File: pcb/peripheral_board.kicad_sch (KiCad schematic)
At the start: 2 parts

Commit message: Continue work on PCBs.
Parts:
- added SW3: SW_RST, Button_Switch_THT:SW_PUSH_6mm, symbol Switch:SW_Push
- added U3: ~, excelsior:MCP23017_Breakout, symbol excelsior:MCP23017_Breakout
- J3, J4: value ~ -> HDMI Breakout
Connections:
- net VBUS: now reaches J4.00 (VBUS)
- net VBUS: now also J3.00 (VBUS), U3.00 (VBUS)
- net MISO: now reaches J4.01 (P01)
- net MISO: now also J3.01 (P01)
- net CS0: now reaches J4.02 (P02)
- net CS0: now also J3.02 (P02)
- net SCK: now reaches J4.03 (P03)
- net SCK: now also J3.03 (P03)
- net CS1: now reaches J4.04 (P04)
- net CS1: now also J3.04 (P04)
- net MOSI: now reaches J4.05 (P05)
- net MOSI: now also J3.05 (P05)
- net CS2: now reaches J4.06 (P06)
- net CS2: now also J3.06 (P06)
- net SDA: now reaches J4.07 (P07)
- net SDA: now also J3.07 (P07), U3.03 (SDA)
- net CS3: now reaches J4.08 (P08)
- net CS3: now also J3.08 (P08)
- net SCL: now reaches J4.09 (P09)
- net SCL: now also J3.09 (P09), U3.02 (SCL)
- net CS4: now reaches J4.10 (P10)
- net CS4: now also J3.10 (P10)
- net INTA1: now reaches J4.11 (P11)
- net INTA1: now also J3.11 (P11), U3.25 (INTA)
- net CS5: now reaches J4.12 (P12)
- net CS5: now also J3.12 (P12)
- net INTB1: now reaches J4.13 (P13)
- net INTB1: now also J3.13 (P13), U3.24 (INTB)
- net CS6: now reaches J4.14 (P14)
- net CS6: now also J3.14 (P14)
- net INTA2: now reaches J4.15 (P15)
- net INTA2: now also J3.15 (P15)
- net CS7: now reaches J4.16 (P16)
- net CS7: now also J3.16 (P16)
- net GND: now reaches J4.G (GND)
- net GND: now also J3.G (GND), SW3.1, U3.01 (GND)
- new net: SW3.2, U3.04 (RST)
- new net C00: U3.20 (GPB0)
- new net C01: U3.19 (GPB1)
- new net C02: U3.18 (GPB2)
- new net C03: U3.17 (GPB3)
- new net C04: U3.16 (GPB4)
- new net C05: U3.15 (GPB5)
- new net GPA6: U3.11 (GPA6)
- new net GPA7: U3.12 (GPA7)
- new net GPB6: U3.14 (GPB6)
- new net GPB7: U3.13 (GPB7)
- new net INTB2: J3.19 (P19), J4.19 (P19)
- new net R00: U3.05 (GPA0)
- new net R01: U3.06 (GPA1)
- new net R02: U3.07 (GPA2)
- new net R03: U3.08 (GPA3)
- new net R04: U3.09 (GPA4)
- new net R05: U3.10 (GPA5)
- no-connect marks 0 -> 3

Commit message: Continue work on PCBs.
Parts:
- J3, J4: value HDMI Breakout -> Pogo Pin Connector; footprint excelsior:HDMI_Breakout -> Connector_PinHeader_2.54mm:PinHeader_1x12_P2.54mm_Vertical; symbol excelsior:HDMI_Breakout -> Connector_Generic:Conn_01x12
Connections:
- net CS4 is gone; now on net CS0: J3.10 (Pin_10), J4.10 (Pin_10)
- net CS5 is gone; now on net CS2: J3.12 (Pin_12), J4.12 (Pin_12)
- net CS0: no longer J3.02 (P02), J4.02 (P02)
- net CS1: now also J3.11 (Pin_11), J4.11 (Pin_11); no longer J3.04 (P04), J4.04 (P04)
- net CS2: no longer J3.06 (P06), J4.06 (P06)
- net GND: no longer J3.G (GND), J4.G (GND)
- net INTA1: now also J3.6 (Pin_6), J4.6 (Pin_6); no longer J3.11 (P11), J4.11 (P11)
- net INTA2: now also J3.8 (Pin_8), J4.8 (Pin_8); no longer J3.15 (P15), J4.15 (P15)
- net INTB1: now also J3.7 (Pin_7), J4.7 (Pin_7); no longer J3.13 (P13), J4.13 (P13)
- net INTB2: now also J3.9 (Pin_9), J4.9 (Pin_9); no longer J3.19 (P19), J4.19 (P19)
- net MISO: now also J3.1 (Pin_1), J4.1 (Pin_1); no longer J3.01 (P01), J4.01 (P01)
- net MOSI: now also J3.3 (Pin_3), J4.3 (Pin_3); no longer J3.05 (P05), J4.05 (P05)
- net SCK: now also J3.2 (Pin_2), J4.2 (Pin_2); no longer J3.03 (P03), J4.03 (P03)
- net SCL: now also J3.5 (Pin_5), J4.5 (Pin_5); no longer J3.09 (P09), J4.09 (P09)
- net SDA: now also J3.4 (Pin_4), J4.4 (Pin_4); no longer J3.07 (P07), J4.07 (P07)
- net VBUS: no longer J3.00 (VBUS), J4.00 (VBUS)
- removed net CS3: J3.08 (P08), J4.08 (P08)
- removed net CS6: J3.14 (P14), J4.14 (P14)
- removed net CS7: J3.16 (P16), J4.16 (P16)

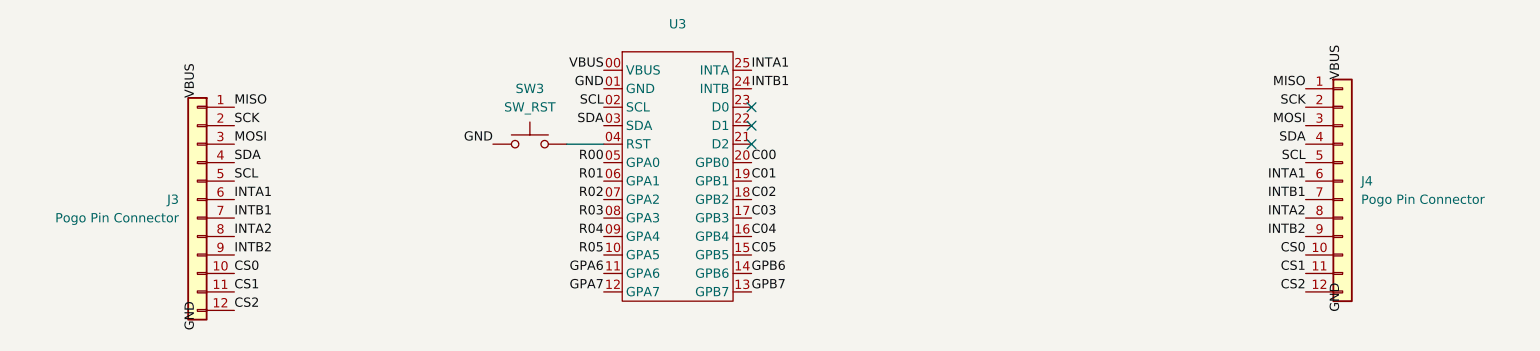
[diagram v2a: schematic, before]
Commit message: - Update main Readme. - Add folders for case CAD and KMK files. - In the PCBs, fix VBUS and GND being removed from connectors. - Add PCB readme.
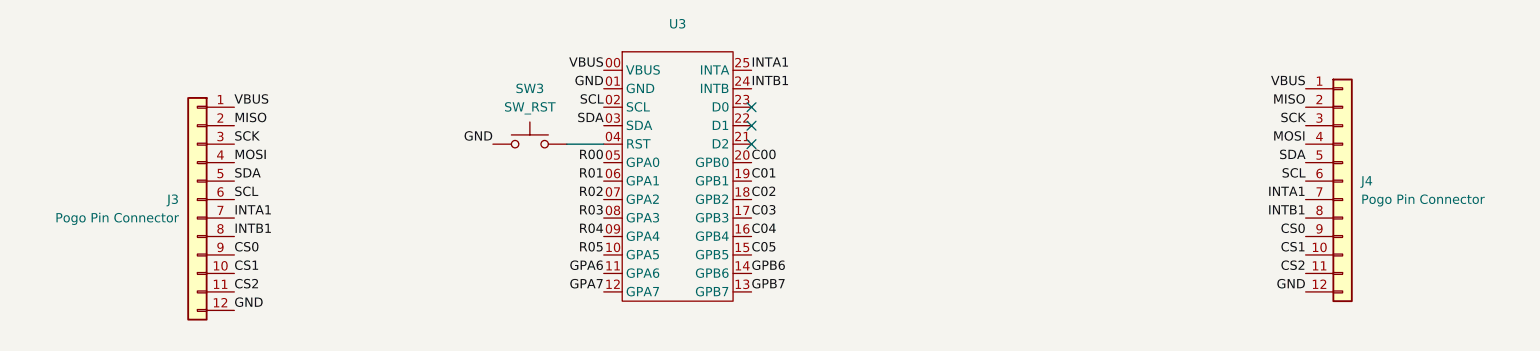
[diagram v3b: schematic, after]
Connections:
- net INTA2 is gone; now on net INTB1: J3.8 (Pin_8), J4.8 (Pin_8)
- net INTB2 is gone; now on net CS0: J3.9 (Pin_9), J4.9 (Pin_9)
- net CS0: no longer J3.10 (Pin_10), J4.10 (Pin_10)
- net CS1: now also J3.10 (Pin_10), J4.10 (Pin_10); no longer J3.11 (Pin_11), J4.11 (Pin_11)
- net CS2: now also J3.11 (Pin_11), J4.11 (Pin_11); no longer J3.12 (Pin_12), J4.12 (Pin_12)
- net GND: now also J3.12 (Pin_12), J4.12 (Pin_12)
- net INTA1: now also J3.7 (Pin_7), J4.7 (Pin_7); no longer J3.6 (Pin_6), J4.6 (Pin_6)
- net INTB1: no longer J3.7 (Pin_7), J4.7 (Pin_7)
- net MISO: now also J3.2 (Pin_2), J4.2 (Pin_2); no longer J3.1 (Pin_1), J4.1 (Pin_1)
- net MOSI: now also J3.4 (Pin_4), J4.4 (Pin_4); no longer J3.3 (Pin_3), J4.3 (Pin_3)
- net SCK: now also J3.3 (Pin_3), J4.3 (Pin_3); no longer J3.2 (Pin_2), J4.2 (Pin_2)
- net SCL: now also J3.6 (Pin_6), J4.6 (Pin_6); no longer J3.5 (Pin_5), J4.5 (Pin_5)
- net SDA: now also J3.5 (Pin_5), J4.5 (Pin_5); no longer J3.4 (Pin_4), J4.4 (Pin_4)
- net VBUS: now also J3.1 (Pin_1), J4.1 (Pin_1)
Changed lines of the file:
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@@
-		)
-	)
-	(label "INTA1"
-		(at 233.68 86.36 180)
-		(effects
-			(font
-				(size 1.27 1.27)
-			)
-			(justify right bottom)
-		)
-	)
-	(label "MOSI"
-		(at 233.68 78.74 180)
-		(effects
-			(font
-				(size 1.27 1.27)
-			)
-			(justify right bottom)
 		)
 	)
@@
 		)
 	)
-	(label "GND"
-		(at 238.76 100.33 270)
-		(effects
-			(font
-				(size 1.27 1.27)
-			)
-			(justify right bottom)
-		)
-	)
-	(label "INTB1"
-		(at 233.68 88.9 180)
-		(effects
-			(font
-				(size 1.27 1.27)
-			)
-			(justify right bottom)
+	(label "INTA1"
+		(at 86.36 91.44 0)
+		(effects
+			(font
+				(size 1.27 1.27)
+			)
+			(justify left bottom)
 		)
 	)
@@
 		)
 	)
-	(label "VBUS"
-		(at 238.76 72.39 90)
-		(effects
-			(font
-				(size 1.27 1.27)
-			)
-			(justify left bottom)
+	(label "CS1"
+		(at 233.68 96.52 180)
+		(effects
+			(font
+				(size 1.27 1.27)
+			)
+			(justify right bottom)
+		)
+	)
+	(label "SDA"
+		(at 86.36 86.36 0)
+		(effects
+			(font
+				(size 1.27 1.27)
+			)
+			(justify left bottom)
+		)
+	)
+	(label "GND"
+		(at 233.68 101.6 180)
+		(effects
+			(font
+				(size 1.27 1.27)
+			)
+			(justify right bottom)
 		)
 	)
@@
 		)
 	)
+	(label "SCL"
+		(at 86.36 88.9 0)
+		(effects
+			(font
+				(size 1.27 1.27)
+			)
+			(justify left bottom)
+		)
+	)
+	(label "SDA"
+		(at 233.68 83.82 180)
+		(effects
+			(font
+				(size 1.27 1.27)
+			)
+			(justify right bottom)
+		)
+	)
+	(label "CS0"
+		(at 233.68 93.98 180)
+		(effects
+			(font
+				(size 1.27 1.27)
+			)
+			(justify right bottom)
+		)
+	)
 	(label "INTB1"
-		(at 86.36 91.44 0)
-		(effects
-			(font
-				(size 1.27 1.27)
-			)
-			(justify left bottom)
-		)
-	)
-	(label "SCL"
-		(at 86.36 86.36 0)
+		(at 86.36 93.98 0)
 		(effects
 			(font
@@
 		)
 	)
+	(label "MOSI"
+		(at 233.68 81.28 180)
+		(effects
+			(font
+				(size 1.27 1.27)
+			)
+			(justify right bottom)
+		)
+	)
 	(label "C02"
 		(at 157.48 88.9 0)
@@
 		)
 	)
-	(label "MISO"
+	(label "VBUS"
 		(at 233.68 73.66 180)
 		(effects
@@
 			)
 			(justify right bottom)
-		)
-	)
-	(label "SCK"
-		(at 86.36 78.74 0)
-		(effects
-			(font
-				(size 1.27 1.27)
-			)
-			(justify left bottom)
-		)
-	)
-	(label "SCK"
-		(at 233.68 76.2 180)
-		(effects
-			(font
-				(size 1.27 1.27)
-			)
-			(justify right bottom)
-		)
-	)
-	(label "CS1"
-		(at 233.68 99.06 180)
-		(effects
-			(font
-				(size 1.27 1.27)
-			)
-			(justify right bottom)
-		)
-	)
-	(label "VBUS"
-		(at 81.28 74.93 90)
-		(effects
-			(font
-				(size 1.27 1.27)
-			)
-			(justify left bottom)
 		)
 	)
@@
 	)
 	(label "CS2"
-		(at 86.36 104.14 0)
-		(effects
-			(font
-				(size 1.27 1.27)
-			)
-			(justify left bottom)
-		)
-	)
-	(label "INTB2"
-		(at 233.68 93.98 180)
-		(effects
-			(font
-				(size 1.27 1.27)
-			)
-			(justify right bottom)
-		)
-	)
-	(label "MISO"
-		(at 86.36 76.2 0)
+		(at 86.36 101.6 0)
+		(effects
+			(font
+				(size 1.27 1.27)
+			)
+			(justify left bottom)
+		)
+	)
+	(label "CS1"
+		(at 86.36 99.06 0)
 		(effects
 			(font
@@
 		)
 	)
-	(label "CS2"
-		(at 233.68 101.6 180)
+	(label "SCK"
+		(at 233.68 78.74 180)
 		(effects
 			(font
@@
 		)
 	)
-	(label "INTA2"
-		(at 86.36 93.98 0)
-		(effects
-			(font
-				(size 1.27 1.27)
-			)
-			(justify left bottom)
+	(label "CS2"
+		(at 233.68 99.06 180)
+		(effects
+			(font
+				(size 1.27 1.27)
+			)
+			(justify right bottom)
 		)
 	)
@@
 		)
 	)
+	(label "MOSI"
+		(at 86.36 83.82 0)
+		(effects
+			(font
+				(size 1.27 1.27)
+			)
+			(justify left bottom)
+		)
+	)
 	(label "R05"
 		(at 137.16 96.52 180)
@@
 		)
 	)
+	(label "MISO"
+		(at 233.68 76.2 180)
+		(effects
+			(font
+				(size 1.27 1.27)
+			)
+			(justify right bottom)
+		)
+	)
 	(label "VBUS"
 		(at 137.16 71.12 180)
@@
 		)
 	)
+	(label "SCL"
+		(at 233.68 86.36 180)
+		(effects
+			(font
+				(size 1.27 1.27)
+			)
+			(justify right bottom)
+		)
+	)
+	(label "VBUS"
+		(at 86.36 76.2 0)
+		(effects
+			(font
+				(size 1.27 1.27)
+			)
+			(justify left bottom)
+		)
+	)
+	(label "INTB1"
+		(at 233.68 91.44 180)
+		(effects
+			(font
+				(size 1.27 1.27)
+			)
+			(justify right bottom)
+		)
+	)
 	(label "INTB1"
 		(at 157.48 73.66 0)
@@
 		)
 	)
-	(label "SDA"
-		(at 233.68 81.28 180)
-		(effects
-			(font
-				(size 1.27 1.27)
-			)
-			(justify right bottom)
-		)
-	)
-	(label "INTA1"
-		(at 86.36 88.9 0)
-		(effects
-			(font
-				(size 1.27 1.27)
-			)
-			(justify left bottom)
-		)
-	)
 	(label "CS0"
-		(at 86.36 99.06 0)
+		(at 86.36 96.52 0)
 		(effects
 			(font
@@
 		)
 	)
-	(label "CS1"
-		(at 86.36 101.6 0)
-		(effects
-			(font
-				(size 1.27 1.27)
-			)
-			(justify left bottom)
-		)
-	)
-	(label "INTB2"
-		(at 86.36 96.52 0)
-		(effects
-			(font
-				(size 1.27 1.27)
-			)
-			(justify left bottom)
-		)
-	)
-	(label "SCL"
-		(at 233.68 83.82 180)
-		(effects
-			(font
-				(size 1.27 1.27)
-			)
-			(justify right bottom)
-		)
-	)
 	(label "GND"
-		(at 81.28 102.87 270)
-		(effects
-			(font
-				(size 1.27 1.27)
-			)
-			(justify right bottom)
+		(at 86.36 104.14 0)
+		(effects
+			(font
+				(size 1.27 1.27)
+			)
+			(justify left bottom)
 		)
 	)
@@
 		)
 	)
+	(label "SCK"
+		(at 86.36 81.28 0)
+		(effects
+			(font
+				(size 1.27 1.27)
+			)
+			(justify left bottom)
+		)
+	)
 	(label "GPB6"
 		(at 157.48 99.06 0)
@@
 		)
 	)
-	(label "SDA"
-		(at 86.36 83.82 0)
-		(effects
-			(font
-				(size 1.27 1.27)
-			)
-			(justify left bottom)
-		)
-	)
 	(label "SCL"
 		(at 137.16 76.2 180)
@@
 		)
 	)
-	(label "CS0"
-		(at 233.68 96.52 180)
-		(effects
-			(font
-				(size 1.27 1.27)
-			)
-			(justify right bottom)
-		)
-	)
-	(label "MOSI"
-		(at 86.36 81.28 0)
-		(effects
-			(font
-				(size 1.27 1.27)
-			)
-			(justify left bottom)
-		)
-	)
 	(label "GPA7"
 		(at 137.16 101.6 180)
@@
 		)
 	)
-	(label "INTA2"
-		(at 233.68 91.44 180)
-		(effects
-			(font
-				(size 1.27 1.27)
-			)
-			(justify right bottom)
-		)
-	)
+	(label "INTA1"
+		(at 233.68 88.9 180)
+		(effects
+			(font
+				(size 1.27 1.27)
+			)
+			(justify right bottom)
+		)
+	)
+	(label "MISO"
+		(at 86.36 78.74 0)
+		(effects
+			(font
+				(size 1.27 1.27)
+			)
+			(justify left bottom)
+		)
+	)
